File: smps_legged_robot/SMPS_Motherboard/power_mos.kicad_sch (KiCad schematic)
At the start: 12 parts, among them Q1601 PSMN4R8-100BSEJ, Q1602 PSMN4R8-100BSEJ, Q1603 PSMN4R8-100BSEJ, Q1604 PSMN4R8-100BSEJ, Q1605 PSMN4R8-100BSEJ, Q1606 PSMN4R8-100BSEJ

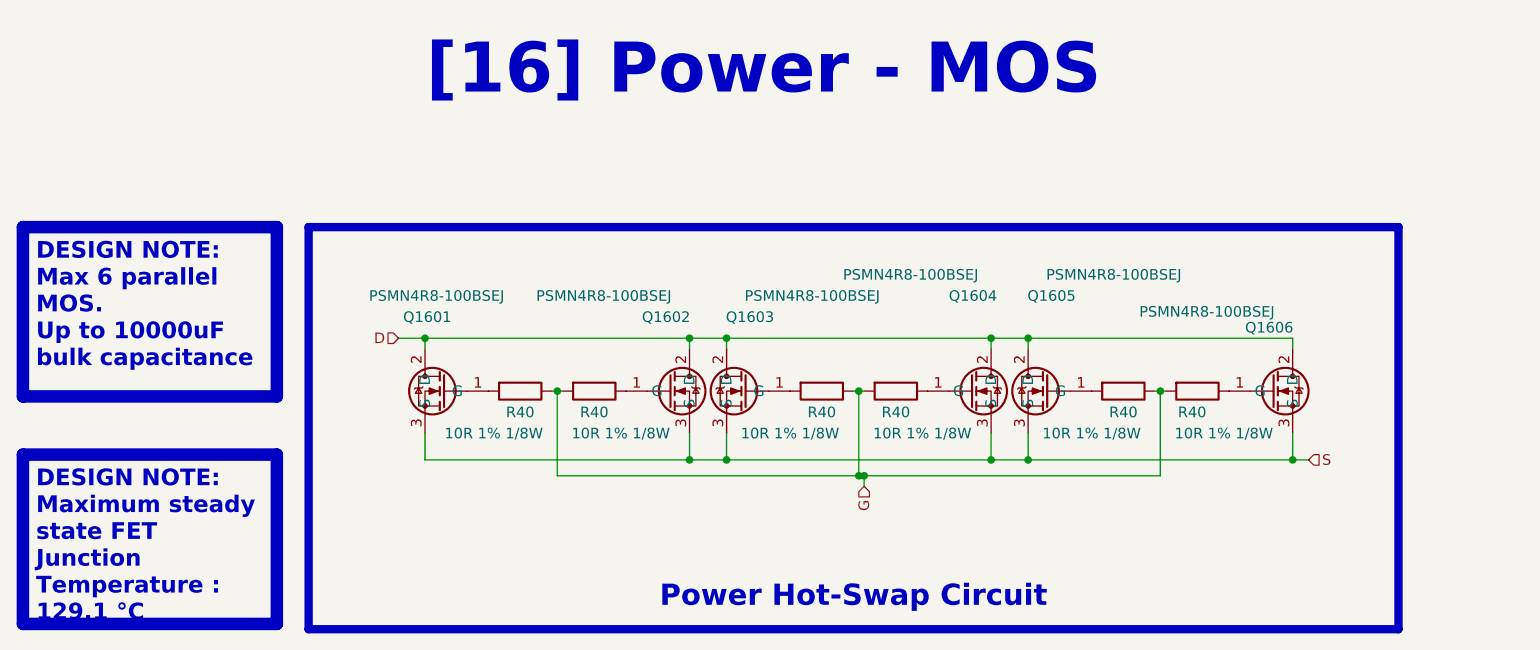
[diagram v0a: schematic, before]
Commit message: Rev 1.0 of smps finished -> waiting for verification
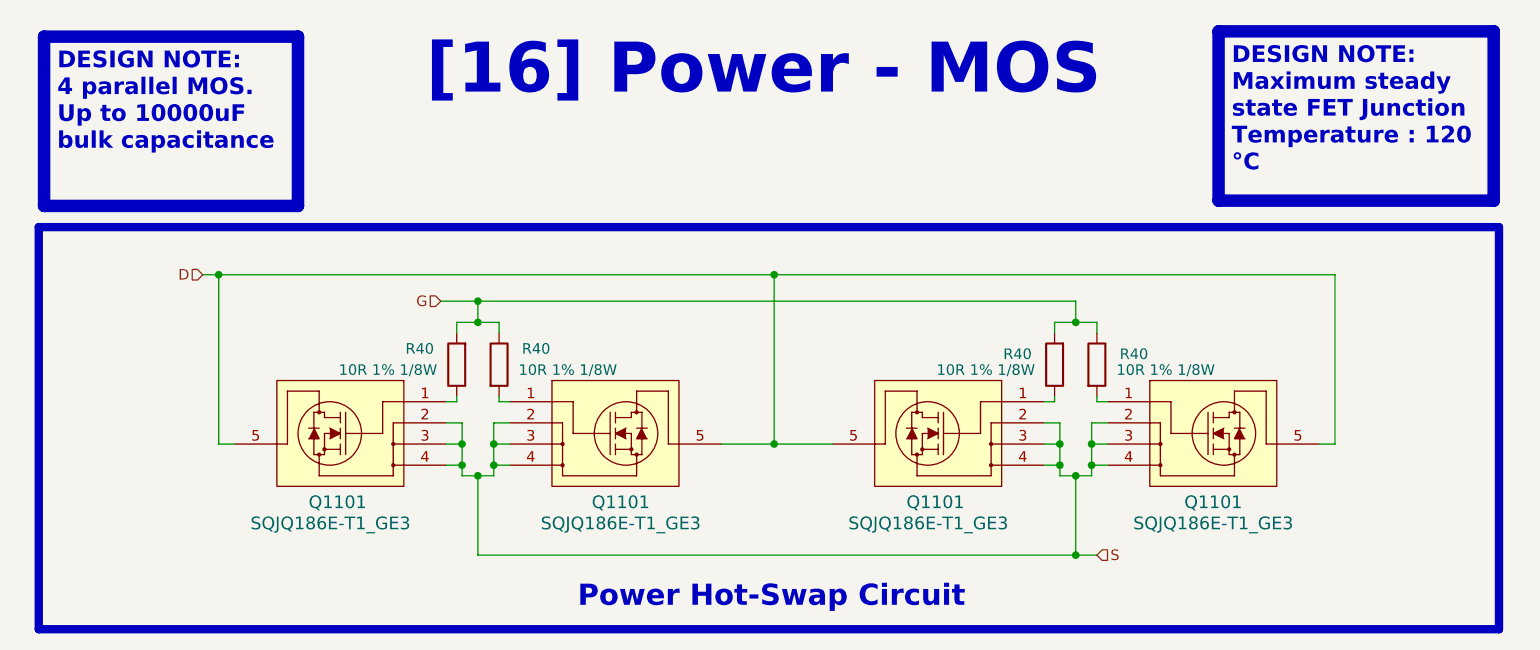
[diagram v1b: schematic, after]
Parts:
- removed Q1601, Q1602, Q1603, Q1604, Q1605, Q1606: PSMN4R8-100BSEJ, 0_diode_smd:PHB45NQ15T118, symbol PSMN4R8-100BSEJ:PSMN4R8-100BSEJ
- removed R40 (x2): 10R 1% 1/8W, 0_resistor_smd:R_0805_2012_DensityHigh, symbol Device:R
- added Q1101 (x4): SQJQ186E-T1_GE3, 0_transistor_fet:POWERPAK8X8L_VIS, symbol 2024-04-07_09-28-25:SQJQ186E-T1_GE3
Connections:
- net D: now also Q1101.5, Q1101.5, Q1101.5, Q1101.5
- net G: now also R40.1, R40.1, R40.2, R40.2; no longer R40.1, R40.1, R40.2, R40.2
- net S: now also Q1101.2, Q1101.2, Q1101.2, Q1101.2, Q1101.3, Q1101.3, Q1101.3, Q1101.3, Q1101.4, Q1101.4, Q1101.4, Q1101.4
- new net: Q1101.1, R40.2 (x2)
- new net: Q1101.1, R40.1 (x2)
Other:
- moved on the sheet: R40
